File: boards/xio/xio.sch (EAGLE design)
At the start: 249 parts, among them CN3 J00-0065NL, U2 LAN8742A-CZ, X2 USB-A, Y1 NX3225SA-12.000MHZ-STD-CSR-1, Y2 NX3225SA-12.000MHZ-STD-CSR-1, Y3 NX3225SA-25.000MHZ-STD-CSR-1

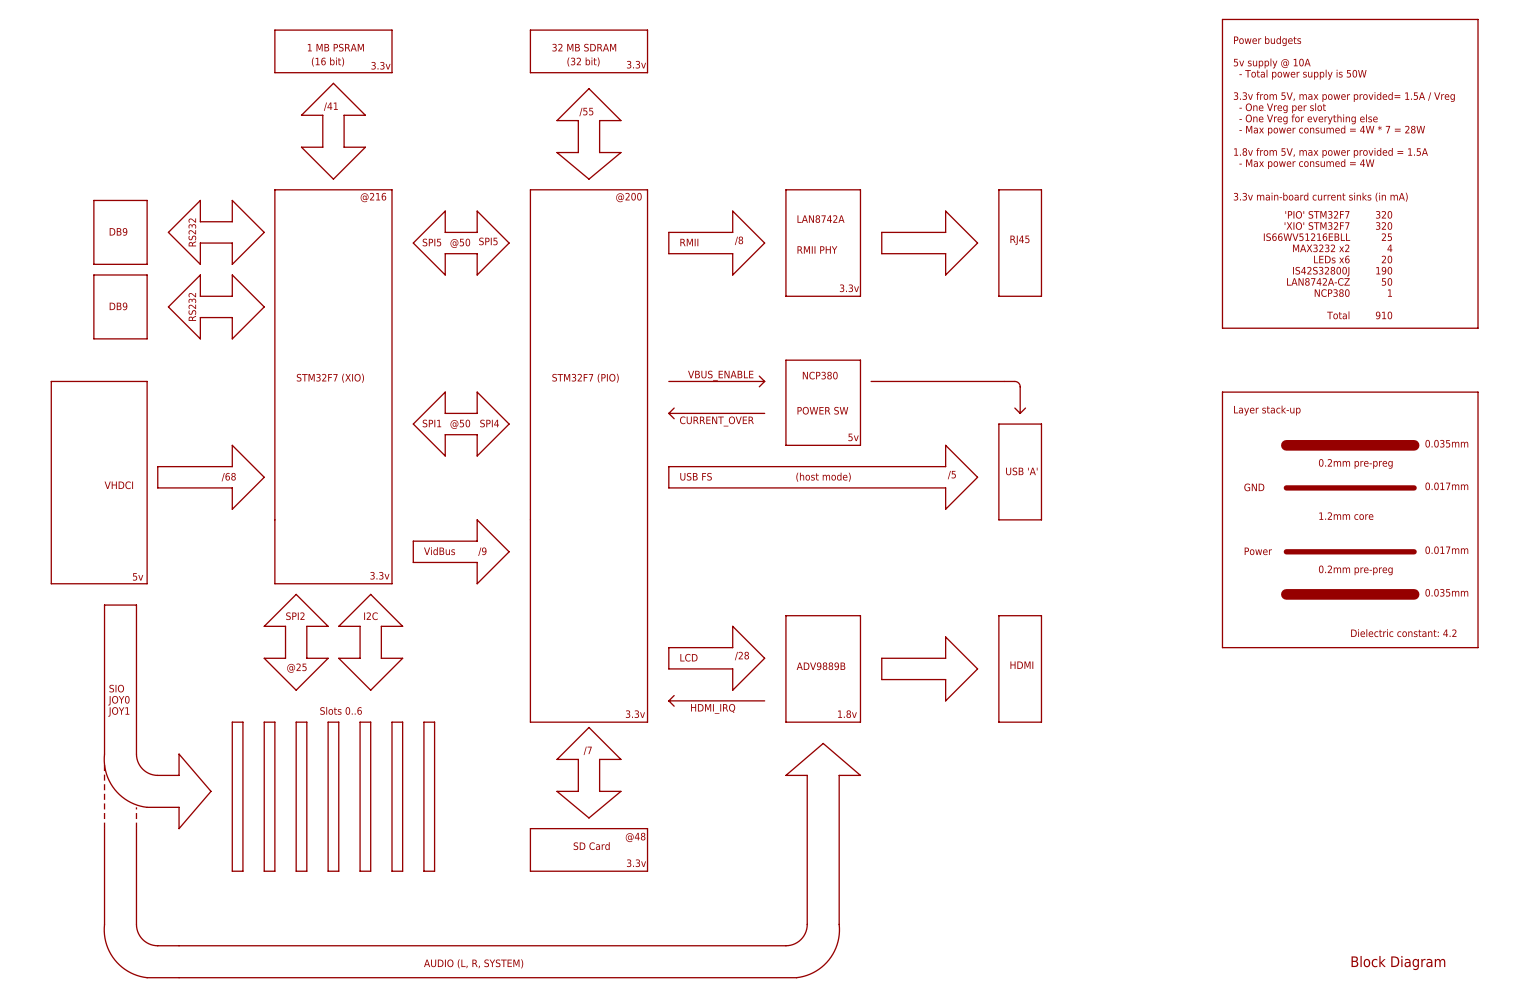
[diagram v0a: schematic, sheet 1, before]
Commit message: Add some more documentation to the schematic…
 - Add a diagram showing the bus cycle waveform
 - Add a diagram showing the audio level translation
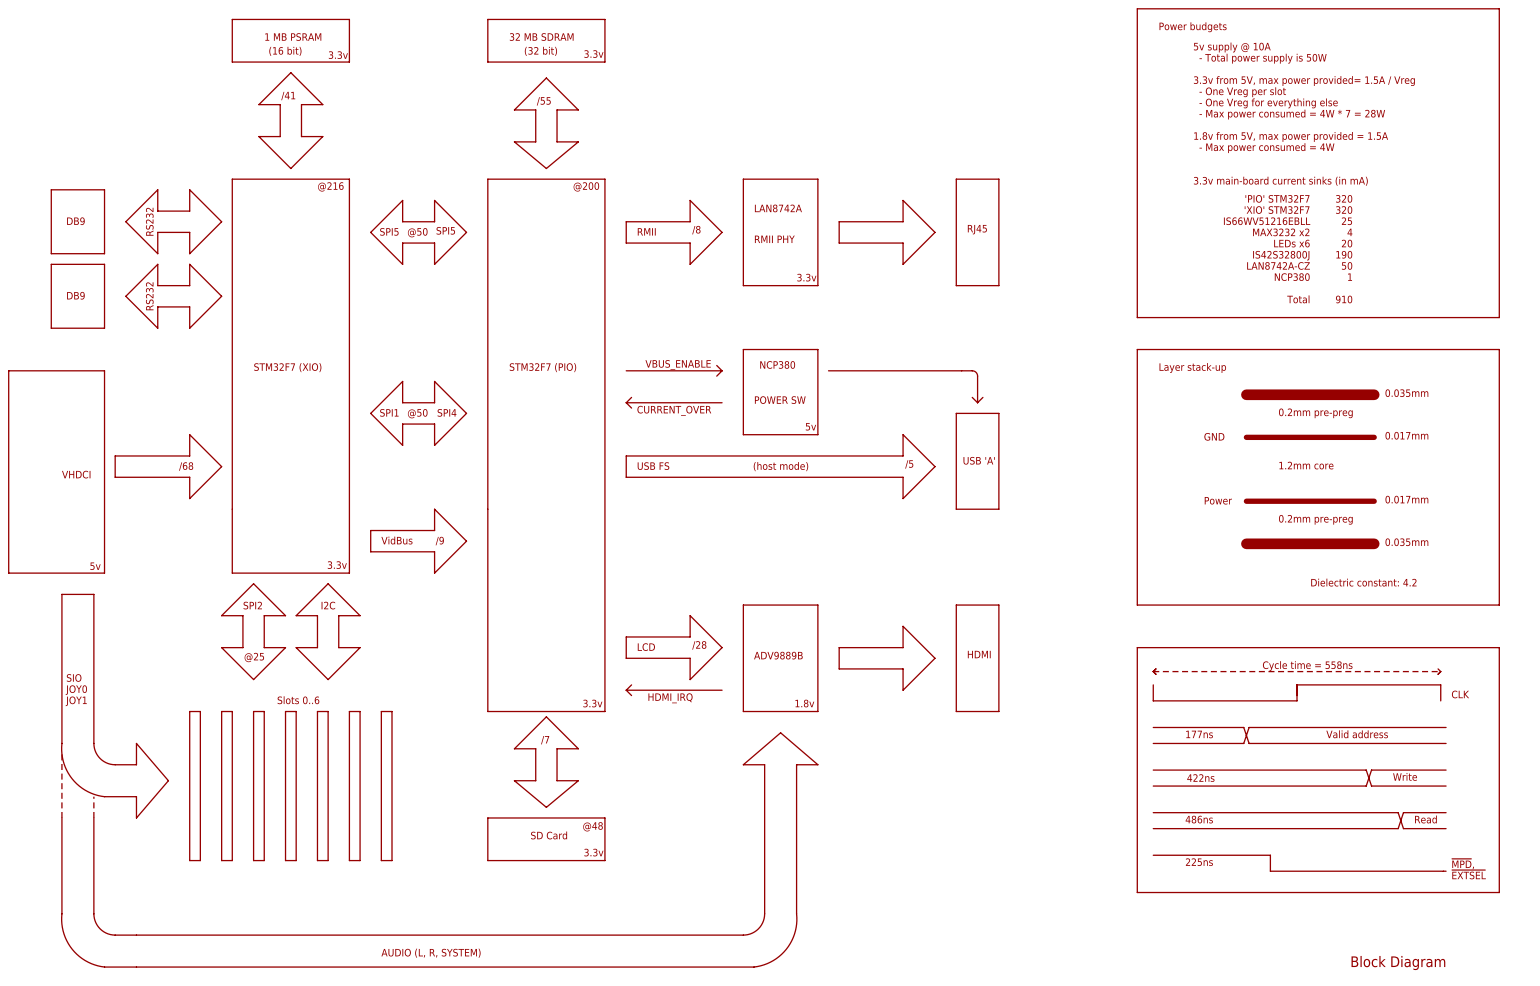
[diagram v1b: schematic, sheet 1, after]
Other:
- note added: "!MPD!, !EXTSEL!"
- note added: "+0.4v"
- note added: "+1.25v"
- note added: "+2.05v"
- note added: "-0.4v"
- note added: "0v"
- note added: "1.65v"
- note added: "177ns"
- note added: "225ns"
- note added: "422ns"
- note added: "486ns"
- note added: "5v supply @ 10A - Total power supply is 50W 3.3v from 5V, max power provided= 1.5A / Vreg - One Vreg per slot - One Vreg for everything else - Max power consumed = 4W * 7 = 28W 1.8v from 5V, max power provided = 1.5A - Max power consumed = 4W 3.3v main-board current sinks (in mA)"
- note added: "CLK"
- note added: "Cycle time = 558ns"
- note added: "Power budgets"
- note added: "Read"
- note added: "Valid address"
- note added: "Write"
- note removed: "Power budgets 5v supply @ 10A - Total power supply is 50W 3.3v from 5V, max power provided= 1.5A / Vreg - One Vreg per slot - One Vreg for everything else - Max power consumed = 4W * 7 = 28W 1.8v from 5V, max power provided = 1.5A - Max power consumed = 4W 3.3v main-board current sinks (in mA)"

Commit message: Some more documentation improvements
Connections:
- net N$105 renamed XIO_RAM_A17
- net N$106 renamed XIO_RAM_A18
- net N$107 renamed XIO_RAM_D0
- net N$108 renamed XIO_RAM_D1
- net N$109 renamed XIO_RAM_D2
- net N$110 renamed XIO_RAM_D3
- net N$111 renamed XIO_RAM_D4
- net N$112 renamed XIO_RAM_D5
- net N$113 renamed XIO_RAM_D6
- net N$114 renamed XIO_RAM_D7
- net N$115 renamed XIO_RAM_D8
- net N$116 renamed XIO_RAM_D9
- net N$117 renamed XIO_RAM_D10
- net N$118 renamed XIO_RAM_D11
- net N$119 renamed XIO_RAM_D12
- net N$120 renamed XIO_RAM_D13
- net N$121 renamed XIO_RAM_D14
- net N$122 renamed XIO_RAM_D15
- net N$123 renamed XIO_RAM_!OE!
- net N$124 renamed XIO_RAM_!WE!
- net N$125 renamed XIO_RAM_!LB!
- net N$126 renamed XIO_RAM_!UB!
- net N$127 renamed XIO_RAM_!CS!
- net N$19 renamed XIO_RAM_A0
- net N$22 renamed XIO_RAM_A1
- net N$51 renamed XIO_RAM_A2
- net N$53 renamed XIO_RAM_A3
- net N$54 renamed XIO_RAM_A4
- net N$55 renamed XIO_RAM_A5
- net N$56 renamed XIO_RAM_A6
- net N$57 renamed XIO_RAM_A7
- net N$58 renamed XIO_RAM_A8
- net N$59 renamed XIO_RAM_A9
- net N$60 renamed XIO_RAM_A10
- net N$61 renamed XIO_RAM_A11
- net N$63 renamed XIO_RAM_A12
- net N$65 renamed XIO_RAM_A13
- net N$66 renamed XIO_RAM_A14
- net N$72 renamed XIO_RAM_A15
- net N$73 renamed XIO_RAM_A16
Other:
- moved on the sheet: PIO-AUDIO

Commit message: Documentation tweaks
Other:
- note added: "Place pull-ups close to card socket"
- note added: "Question: Do I need line drivers on the 18 could-be-output lines ? (RSRVD[0..2], !MPD!,!EXSEL!,!IRQ!,RD4,RD5,!RST!,!HALT!,D[0..7]) According to datasheet (p97) - Max current per pin: 25mA - Overall max current: 120mA"
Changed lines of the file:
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@@
 <text x="160.02" y="58.42" size="2.54" layer="97">Cartridge
 Port Header</text>
+<text x="93.98" y="-101.6" size="1.778" layer="97">Question: Do I need line drivers on the 18 could-be-output lines ?
+(RSRVD[0..2], !MPD!,!EXSEL!,!IRQ!,RD4,RD5,!RST!,!HALT!,D[0..7])
+According to datasheet (p97)
+   - Max current per pin: 25mA
+   - Overall max current: 120mA</text>
 </plain>
 <instances>
@@
 <text x="-7.62" y="-10.16" size="1.778" layer="94">Unused pins</text>
 <text x="144.78" y="-114.3" size="2.54" layer="94">LEDs, Video-bus, unused</text>
+<text x="-121.92" y="77.47" size="2.1844" layer="96">Ports will drive 3.3mA
+with 1K resistors</text>
 </plain>
 <instances>
@@
 <wire x1="-68.58" y1="30.48" x2="-43.18" y2="30.48" width="0.1524" layer="91"/>
 <pinref part="XIO" gate="-PSRAM" pin="PD4@168"/>
-<label x="-63.5" y="30.48" size="1.778" layer="95"/>
+<label x="-63.5" y="30.734" size="1.778" layer="95"/>
 </segment>
 </net>
@@
 <wire x1="-43.18" y1="22.86" x2="-68.58" y2="22.86" width="0.1524" layer="91"/>
 <pinref part="XIO" gate="-PSRAM" pin="PD5@169"/>
-<label x="-63.5" y="22.86" size="1.778" layer="95"/>
+<label x="-63.5" y="23.114" size="1.778" layer="95"/>
 </segment>
 </net>
@@
 <text x="119.38" y="-69.342" size="1.778" layer="97">+1.25v</text>
 <text x="146.812" y="-66.548" size="1.778" layer="97">1.65v</text>
+<text x="-119.38" y="0" size="1.778" layer="97">Place pull-ups close to card socket</text>
 </plain>
 <instances>

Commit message: Part-way through the revisions after the schematic review
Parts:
- removed I2C_EXT: (no value), pinhead:PINHD-1X4
- removed SPI_EXT_0, SPI_EXT_1, SPI_EXT_2: (no value), pinhead:PINHD-1X5
- added C109, C134, C35, C36, C51, C53, C54, C55, C56, C81, C82, C84, C85, C86, C87, C99: 0.1uF, rcl:C-EUC0402K
- added C52: 4.7uF, rcl:C-EUC0402K
- added C83: 10uF, rcl:C-EUC0402K
- added I2C_EXT0, I2C_EXT1: (no value), pinhead:PINHD-1X4
- added L1, L2, L3: BLM15EG221SN1D, inductors:BLM15HB121SN1
- added R21, R26, R27, R30, R31: 33, rcl:R-EU_R0402
- added R55, R56: 0R, rcl:R-EU_R0402
- added R58, R59, R83, R84, R85, R86, R87, R88: 0, rcl:R-EU_R0402
- added SPI_EXT0, SPI_EXT1, SPI_EXT2: (no value), pinhead:PINHD-2X4
- R51, R52: value 0R -> 33
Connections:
- net N$10 renamed XIO_RX
- net N$21 renamed AUDIO_DATA
- net N$25 renamed AUDIO_SCLK
- net N$37 renamed AUDIO_WORD
- net N$7 renamed XIO_SWDIO
- net N$8 renamed XIO_SWDCLK
- net N$9 renamed XIO_TX
- removed net N$64: R57.1, STM_DBG2.C
- removed net N$67: PIO-LED.PD13@113, STM_DBG2.A
- new net N$10: C38.1, R58.2, V33_0.OUT@3
- new net N$19: LED3.A, R4.2
- new net N$21: R52.2, XIO-VBUS.PJ15@177
- new net N$22: R22.1, STM_DBG1.A
- new net N$25: C40.1, R59.2, V33_1.OUT@3
- new net N$37: C42.1, R83.2, V33_2.OUT@3
- new net N$51: R57.1, STM_DBG2.A
- new net N$53: C44.1, R84.2, V33_3.OUT@3
- new net N$54: C46.1, R85.2, V33_4.OUT@3
- new net N$55: C48.1, R86.2, V33_5.OUT@3
- new net N$56: C50.1, R87.2, V33_6.OUT@3
- new net N$58: C107.1, C108.1, R88.2, VRE18.OUT@3
- new net N$7: R53.2, XIO-POWER.PDR_ON@203
- new net N$8: PIO-POWER.PDR_ON@203, R55.2
- new net N$9: C12.1, R56.2, VREG33.OUT@3
- new net XIO_VDDA: R21.1, XIO-POWER.VDDA@42
- net +3V3: now also C134.2, C52.1, I2C_EXT0.1, I2C_EXT1.1, R19.2, R2.1, R21.2, R22.2, R3.1, R4.1, R53.1, R55.1, R56.1, R57.2, SPI_EXT0.4, SPI_EXT1.4, SPI_EXT2.4; no longer C12.1, PIO-POWER.PDR_ON@203, VREG33.OUT@3, XIO-POWER.PDR_ON@203, XIO-POWER.VDDA@42
- net +5V: now also C35.1, C36.1, C51.1, C53.1, C54.1, C55.1, C56.1, C81.1, C82.1, C83.1
- net 1.8V: now also C84.2, C86.2, C99.2, L1.1, L2.1, L3.1, R88.1; no longer C107.1, C108.1, R51.1, R52.1, R53.1, VRE18.OUT@3
- net AGND: now also C1.2, C13.2, C57.2, C58.2
- net AVDD_9889B: now also C109.2, L3.2; no longer R53.2
- net DVDD_9889B: now also C85.2, L1.2; no longer R51.2
- net GND: now also C109.1, C134.1, C35.2, C36.2, C51.2, C52.2, C53.2, C54.2, C55.2, C56.2, C81.2, C82.2, C83.2, C84.1, C85.1, C86.1, C87.1, C99.1, I2C_EXT0.4, I2C_EXT1.4, R26.2, R27.2, R30.2, R31.1, SPI_EXT0.8, SPI_EXT1.8, SPI_EXT2.8; no longer C1.2, C13.2, C57.2, C58.2, R19.2, R2.2, R22.2, R3.2, R4.2, R57.2
- net I2C_SCL: now also I2C_EXT0.2, I2C_EXT1.2; no longer I2C_EXT.1, I2C_EXT.3
- net I2C_SDA: now also I2C_EXT0.3, I2C_EXT1.3; no longer I2C_EXT.2, I2C_EXT.4
- net N$12: now also LED1.A, R2.2; no longer LED3.A, XIO-LED.PD6@172
- net N$13: now also LED1.C, XIO-LED.PD2@166; no longer LED2.A, XIO-LED.PD3@167
- net N$14: now also LED2.C, XIO-LED.PD3@167; no longer LED1.A, XIO-LED.PD2@166
- net N$15: now also LED3.C, XIO-LED.PD6@172; no longer LED1.C, R4.1
- net N$16: now also LED2.A, R3.2; no longer LED2.C, R3.1
- net N$17: now also STM_DBG0.C; no longer STM_DBG0.A
- net N$18: now also R51.2, XIO-VHDCI.PJ0@65; no longer LED3.C, R2.1
- net N$20: now also R19.1, STM_DBG0.A; no longer PIO-LED.PD12@112, STM_DBG1.A
- net N$26: now also PIO-LED.PD12@112; no longer R22.1
- net N$27: now also PIO-LED.PD13@113, STM_DBG2.C; no longer R19.1, STM_DBG0.C
- net PVDD_9889B: now also C87.2, L2.2; no longer R52.2
- net S1_V33: now also R58.1; no longer C38.1, V33_0.OUT@3
- net S2_V33: now also R59.1; no longer C40.1, V33_1.OUT@3
- net S3_V33: now also R83.1; no longer C42.1, V33_2.OUT@3
- net S4_V33: now also R84.1; no longer C44.1, V33_3.OUT@3
- net S5_V33: now also R85.1; no longer C46.1, V33_4.OUT@3
- net S6_V33: now also R86.1; no longer C48.1, V33_5.OUT@3
- net S7_V33: now also R87.1; no longer C50.1, V33_6.OUT@3
- net SPI_CLK: now also R26.1, SPI_EXT0.1, SPI_EXT1.1, SPI_EXT2.1; no longer SPI_EXT_0.1, SPI_EXT_1.1, SPI_EXT_2.1
- net SPI_IRQ7: now also SPI_EXT0.7; no longer SPI_EXT_0.4
- net SPI_IRQ8: now also SPI_EXT1.7; no longer SPI_EXT_1.4
- net SPI_IRQ9: now also SPI_EXT2.7; no longer SPI_EXT_2.4
- net SPI_MISO: now also R30.1, SPI_EXT0.3, SPI_EXT1.3, SPI_EXT2.3; no longer SPI_EXT_0.2, SPI_EXT_1.2, SPI_EXT_2.2
- net SPI_MOSI: now also R27.1, SPI_EXT0.5, SPI_EXT1.5, SPI_EXT2.5; no longer SPI_EXT_0.3, SPI_EXT_1.3, SPI_EXT_2.3
- net SPI_SS7: now also SPI_EXT0.6; no longer SPI_EXT_0.5
- net SPI_SS8: now also SPI_EXT1.6; no longer SPI_EXT_1.5
- net SPI_SS9: now also SPI_EXT2.6; no longer SPI_EXT_2.5
- net VHDCI_CLK: now also R31.2, R51.1; no longer XIO-VHDCI.PJ0@65
- net VIDBUS_CLK: now also R52.1; no longer XIO-VBUS.PJ15@177
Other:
- note added: "Add termination resistors close to STM32F7"
- note added: "Not used. Tied high"
- note added: "Place termination resistor close to VHDCI connector"
- note added: "Series termination resistor Placed close to destination"
- note added: "Series termination resistor Placed close to source"
- note added: "Use green LEDs"
- note removed: "Ports will drive 3.3mA with 1K resistors"
- note removed: "Question: Does splitting the power rails like this actually help with the power line "cleanliness" ? Should I have separate regulators instead ? In particular, PVDD (for PLL) needs to be clean"
- note removed: "Question: Should I have synchronised clocks via a clock-generator ? - Will the vidbus latch signals on an un-matched clock ? - CPUs are ideally running at different speeds anyway (200, 216 MHz)"
- moved on the sheet: ECI, LED1, LED2, LED3, R2, R23, R3, R4, R47, STM_DBG0, STM_DBG1, STM_DBG2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

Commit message: Latest schematic/board after most things in the review completed
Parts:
- added C135: 120pF, rcl:C-EUC0402K
- added C136: 10nF, rcl:C-EUC0402K
- added C137: 0.1uF, rcl:C-EUC0402K
- added C138: 4.7uF, rcl:C-EUC0402K
- added R89, R90, R92: 10K, rcl:R-EU_R0402
- added RESET_SW: (no value), SparkFun:TAC_SWITCHPTH
- added U$3: TPS3808G33DBVR, sjg-power:TPS3808DBVR
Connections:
- net N$128 renamed PIO_RX
- net N$129 renamed PIO_TX
- net N$130 renamed PIO_SWDCLK
- removed net N$131: PIO-POWER.PA13@147, PIO-SWD.SWDIO@2
- new net !MR!: C136.1, RESET_SW.1, RESET_SW.2, U$3.!MR!@3
- new net N$60: C135.1, U$3.CT@4
- new net PIO_SWDIO: PIO-POWER.PA13@147, PIO-SWD.SWDIO@2, R92.2
- net !RESET!: now also R89.2, U$3.!RESET!@1
- net +3V3: now also C137.1, C138.1, R89.1, R90.1, R92.1, U$3.SENSE@5, U$3.VDD@6
- net GND: now also C135.2, C136.2, C137.2, C138.2, RESET_SW.3, RESET_SW.4, U$3.GND@2
- net XIO_SWDIO: now also R90.2
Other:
- note added: "!MR! has internal pull-up"
- note added: "- Added 'PI' filters for the 3 types of VDD rails - Need ESD ? What to do ?"
- note added: "- Added 0.1uF caps on each of the 5v lines on the cartridge - Do I need line-drivers on the VHDCI output lines ?"
- note added: "- Added 33R termination resistors on SPI:{MISO, MOSI, CLK} - Added +3.3v, GND to both I2C and SPI pinouts"
- note added: "- Added bulk 4.7uF capacitor for SDRAM power"
- note added: "- Added capacitor to +3v3 on SD_SLOT - is 0.1uF sufficient ?"
- note added: "- Added caps on 5v rails on slots. - is 0.1uF sufficient ? - Double-checked slot-id, spi {slave,irq} on each slot"
- note added: "- Added pull-up on SWDIO"
- note added: "- Added resistor in series to power on VDDA - is 33R ok ? - Added pull-ups on /RESET and SWDIO - Added 0-ohm resistors on all power sources"
- note added: "- Added series termination for clock on VIDBUS. - Which end should it be close to (source or destination) - LED direction inverted - Added /RESET switch and voltage supervisor"
- note added: "- LED directions inverted"
- note added: "- Need ESD ? What to do ?"
- note added: "Anoop says "mended to add a filter on micro’s VDDA pin and connect the filter cap between VDDA and VSSA" - need to understand more"
- note added: "Pullups"
- note added: "Reset monitor"
- note added: "the 'E' designation on the MAX3232 indicates that it has ESD protection built in"
- moved on the sheet: C10, C16, C2, C26, C27, C28, C29, C3, C31, C32, C33, C34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
